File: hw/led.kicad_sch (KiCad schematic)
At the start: 24 parts

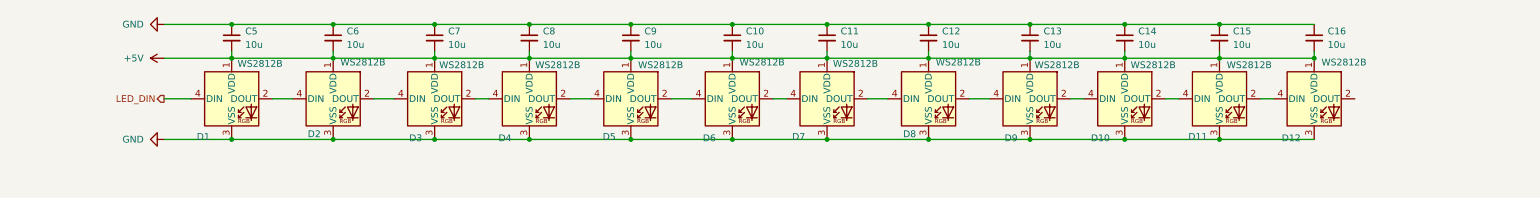
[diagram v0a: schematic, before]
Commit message: Finish power stage, work on other stages
Power stage should be finalised, I've updated LED stage to include a solder jumper, to allow up to half of the LEDs to be removed in the case of power/cost savings
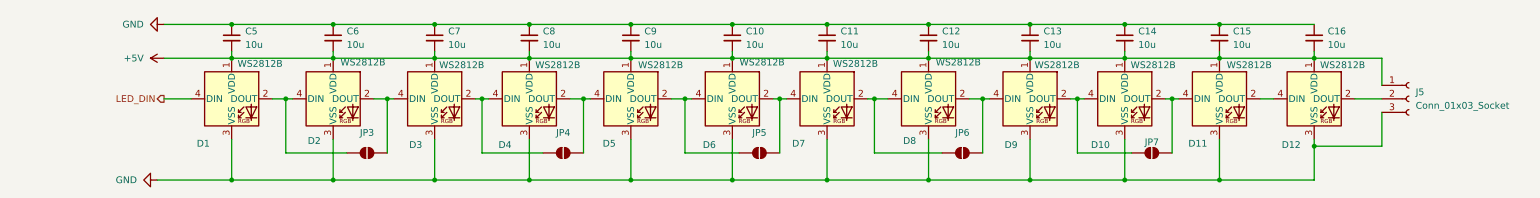
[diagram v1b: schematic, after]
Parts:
- added J5: Conn_01x03_Socket, symbol Connector:Conn_01x03_Socket
- added JP3, JP4, JP5, JP6, JP7: SolderJumper_2_Open, symbol Jumper:SolderJumper_2_Open
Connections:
- net +5V: now also J5.1 (Pin_1)
- net GND: now also J5.3 (Pin_3)
- net at D4.2 (DOUT), D5.4 (DIN): now also JP4.2 (B)
- net at D3.2 (DOUT), D4.4 (DIN): now also JP4.1 (A)
- net at D2.2 (DOUT), D3.4 (DIN): now also JP3.2 (B)
- net at D8.2 (DOUT), D9.4 (DIN): now also JP6.2 (B)
- net at D7.2 (DOUT), D8.4 (DIN): now also JP6.1 (A)
- net at D6.2 (DOUT), D7.4 (DIN): now also JP5.2 (B)
- net at D5.2 (DOUT), D6.4 (DIN): now also JP5.1 (A)
- net at D10.2 (DOUT), D11.4 (DIN): now also JP7.2 (B)
- net at D10.4 (DIN), D9.2 (DOUT): now also JP7.1 (A)
- net at D1.2 (DOUT), D2.4 (DIN): now also JP3.1 (A)
- net at D12.2 (DOUT): now also J5.2 (Pin_2)

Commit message: Work on footprinting and PCB
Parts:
- C11: renamed from C5; footprint (none) -> Capacitor_SMD:C_0805_2012Metric_Pad1.18x1.45mm_HandSolder
- C12: renamed from C6; footprint (none) -> Capacitor_SMD:C_0805_2012Metric_Pad1.18x1.45mm_HandSolder
- C13: renamed from C7; footprint (none) -> Capacitor_SMD:C_0805_2012Metric_Pad1.18x1.45mm_HandSolder
- C14: renamed from C8; footprint (none) -> Capacitor_SMD:C_0805_2012Metric_Pad1.18x1.45mm_HandSolder
- C15: renamed from C9; footprint (none) -> Capacitor_SMD:C_0805_2012Metric_Pad1.18x1.45mm_HandSolder
- C16: renamed from C10; footprint (none) -> Capacitor_SMD:C_0805_2012Metric_Pad1.18x1.45mm_HandSolder
- C17: renamed from C11; footprint (none) -> Capacitor_SMD:C_0805_2012Metric_Pad1.18x1.45mm_HandSolder
- C18: renamed from C12; footprint (none) -> Capacitor_SMD:C_0805_2012Metric_Pad1.18x1.45mm_HandSolder
- C19: renamed from C13; footprint (none) -> Capacitor_SMD:C_0805_2012Metric_Pad1.18x1.45mm_HandSolder
- C20: renamed from C14; footprint (none) -> Capacitor_SMD:C_0805_2012Metric_Pad1.18x1.45mm_HandSolder
- C21: renamed from C15; footprint (none) -> Capacitor_SMD:C_0805_2012Metric_Pad1.18x1.45mm_HandSolder
- C22: renamed from C16; footprint (none) -> Capacitor_SMD:C_0805_2012Metric_Pad1.18x1.45mm_HandSolder
- J4: renamed from J5; footprint (none) -> Connector_JST:JST_VH_B3P-VH-B_1x03_P3.96mm_Vertical
- JP1: renamed from JP3; footprint (none) -> Jumper:SolderJumper-2_P1.3mm_Open_TrianglePad1.0x1.5mm
- JP2: renamed from JP4; footprint (none) -> Jumper:SolderJumper-2_P1.3mm_Open_TrianglePad1.0x1.5mm
- JP3: renamed from JP5; footprint (none) -> Jumper:SolderJumper-2_P1.3mm_Open_TrianglePad1.0x1.5mm
- JP4: renamed from JP6; footprint (none) -> Jumper:SolderJumper-2_P1.3mm_Open_TrianglePad1.0x1.5mm
- JP5: renamed from JP7; footprint (none) -> Jumper:SolderJumper-2_P1.3mm_Open_TrianglePad1.0x1.5mm
- renumbered D9 to D10, D10 to D11, D11 to D12, D12 to D13, D1 to D2, D2 to D3, D3 to D4, D4 to D5, D5 to D6, D6 to D7, D7 to D8, D8 to D9

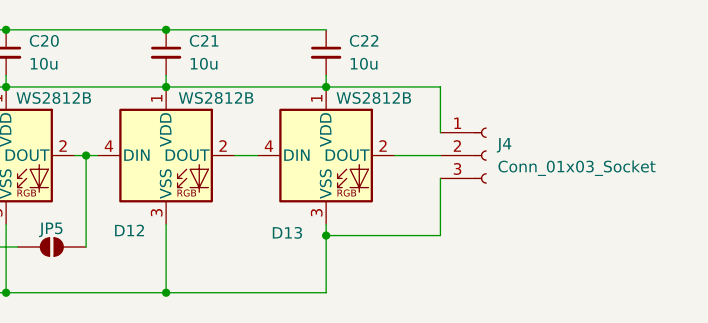
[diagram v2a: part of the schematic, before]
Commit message: Footprinting, begin layout
I've assigned all the footprints except a few, so I've started on layout.
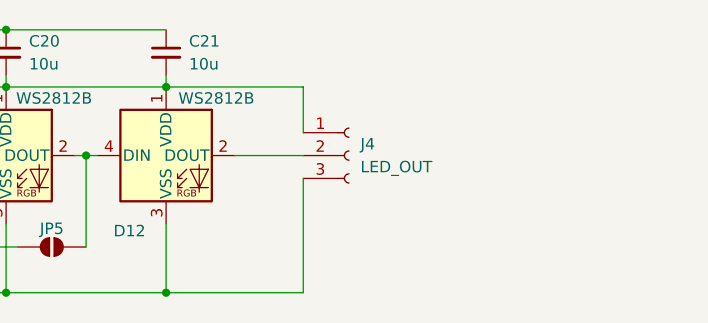
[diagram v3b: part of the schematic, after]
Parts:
- removed C22: 10u, Capacitor_SMD:C_0805_2012Metric_Pad1.18x1.45mm_HandSolder, symbol Device:C_Small
- removed D13: WS2812B, LED_SMD:LED_WS2812B_PLCC4_5.0x5.0mm_P3.2mm, symbol LED:WS2812B
- C11, C12, C13, C14, C15, C16, C17, C18, C19, C20, C21: footprint Capacitor_SMD:C_0805_2012Metric_Pad1.18x1.45mm_HandSolder -> Capacitor_SMD:C_0603_1608Metric
- J4: value Conn_01x03_Socket -> LED_OUT; footprint Connector_JST:JST_VH_B3P-VH-B_1x03_P3.96mm_Vertical -> Connector_JST:JST_EH_B3B-EH-A_1x03_P2.50mm_Vertical
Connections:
- net at J4.2 (Pin_2): now also D12.2 (DOUT)
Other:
- title: (none) -> Weltkatze
- moved on the sheet: J4

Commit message: yes
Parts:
- added C22: 10u, Capacitor_SMD:C_0603_1608Metric, symbol Device:C_Small
- added D13: WS2812B, LED_SMD:LED_WS2812B_PLCC4_5.0x5.0mm_P3.2mm, symbol LED:WS2812B
- added JP8: SolderJumper_2_Open, Jumper:SolderJumper-2_P1.3mm_Open_TrianglePad1.0x1.5mm, symbol Jumper:SolderJumper_2_Open
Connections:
- net +5V: now also C22.2, D13.1 (VDD)
- net GND: now also C22.1, D13.3 (VSS)
- net at J4.2 (Pin_2): now also D13.2 (DOUT), JP8.2 (B); no longer D12.2 (DOUT)
- new net: D12.2 (DOUT), D13.4 (DIN), JP8.1 (A)
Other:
- moved on the sheet: C11, C12, C13, C14, C15, C16, C17, C18, C19, C20, D10, D11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

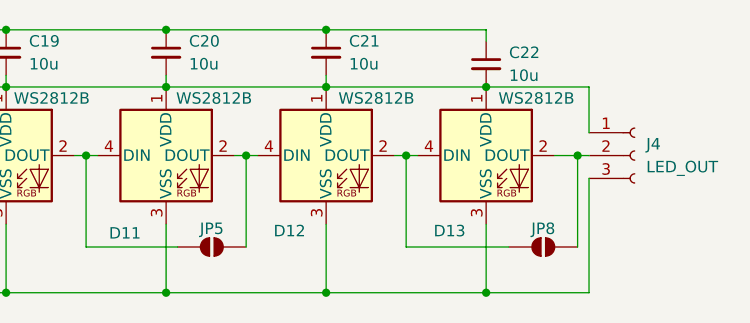
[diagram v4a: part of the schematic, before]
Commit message: I'm actually really stupid.
I made the board sized for a RADIUS of 60mm
and not a DIAMETER of 60mm like the damn fusion model.
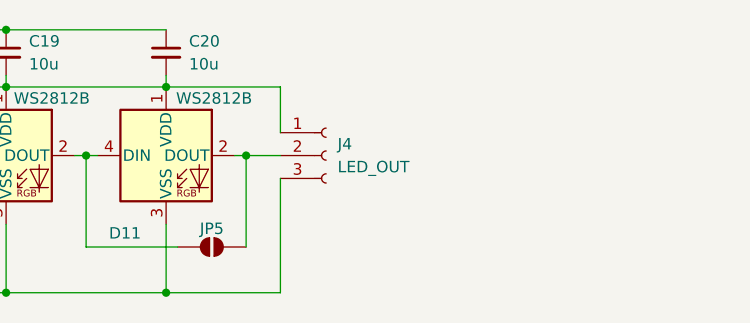
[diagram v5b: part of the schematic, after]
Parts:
- removed C21, C22: 10u, Capacitor_SMD:C_0603_1608Metric, symbol Device:C_Small
- removed D12, D13: WS2812B, LED_SMD:LED_WS2812B_PLCC4_5.0x5.0mm_P3.2mm, symbol LED:WS2812B
- removed JP8: SolderJumper_2_Open, Jumper:SolderJumper-2_P1.3mm_Open_TrianglePad1.0x1.5mm, symbol Jumper:SolderJumper_2_Open
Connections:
- net at J4.2 (Pin_2): now also D11.2 (DOUT), JP5.2 (B)
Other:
- moved on the sheet: J4

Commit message: Update to kicad v9
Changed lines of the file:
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@@
 (kicad_sch
-	(version 20231120)
+	(version 20250114)
 	(generator "eeschema")
-	(generator_version "8.0")
+	(generator_version "9.0")
 	(paper "A4")
 	(title_block

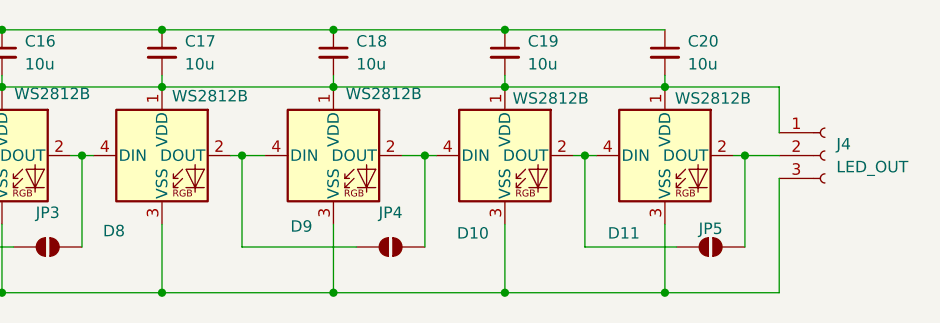
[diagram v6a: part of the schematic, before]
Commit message: Redesign work
I'm going towards a single-sided minimum viable design, so that I only need to place and hotplate one side to  verify function, before adding things like battery and USB by hand.
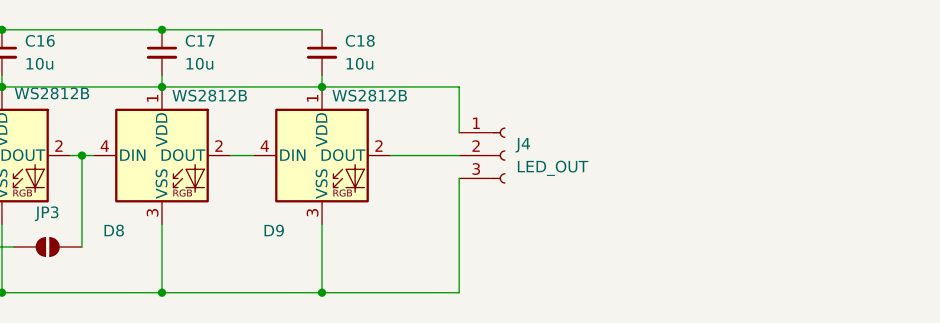
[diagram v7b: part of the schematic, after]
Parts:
- removed C19, C20: 10u, Capacitor_SMD:C_0603_1608Metric, symbol Device:C_Small
- removed D10, D11: WS2812B, LED_SMD:LED_WS2812B_PLCC4_5.0x5.0mm_P3.2mm, symbol LED:WS2812B
- removed JP4, JP5: SolderJumper_2_Open, Jumper:SolderJumper-2_P1.3mm_Open_TrianglePad1.0x1.5mm, symbol Jumper:SolderJumper_2_Open
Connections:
- net at D9.2 (DOUT): now also J4.2 (Pin_2)
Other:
- moved on the sheet: J4
